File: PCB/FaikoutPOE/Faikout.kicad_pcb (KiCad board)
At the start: 2 copper layers, 39 x 65 mm, 91 parts, among them J1 RJ45_LED, J3 S21, J5 Reset, J7 TC2030-USB-NL-DS, M1 Ag9912-LP, P1 Square, P2 Square, P3 Square, P4 Square, P5 Square, P6 Square, P7 Square, P8 Square, Q1 BSS138PS, Q2 BSS138PS, U1 KSZ8851SNL, U2 ESP32-S3-MINI-1, U3 TCMT1100, U5 TCMT1100, U6 TPS62933, Y1 Crystal_GND24

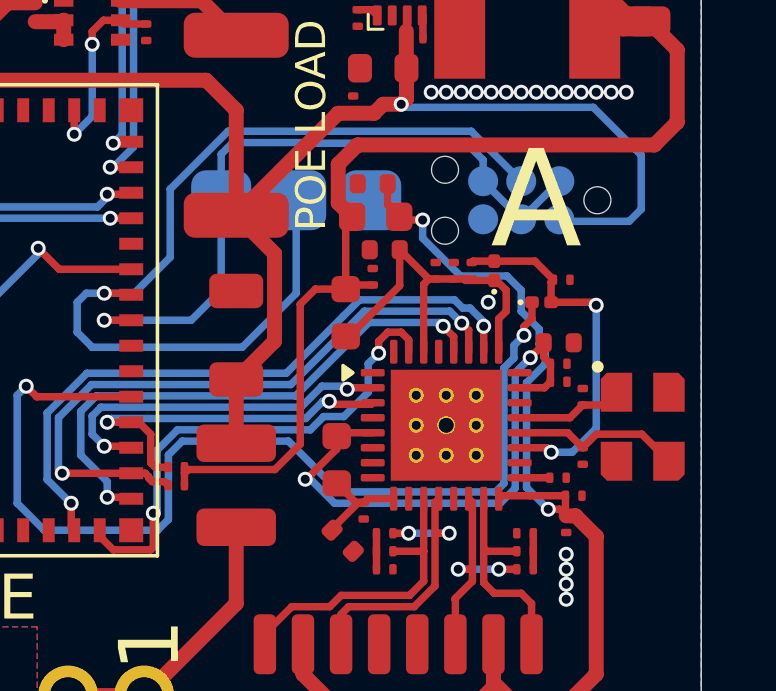
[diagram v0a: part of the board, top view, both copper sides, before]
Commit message: Revised Ethernet footprint
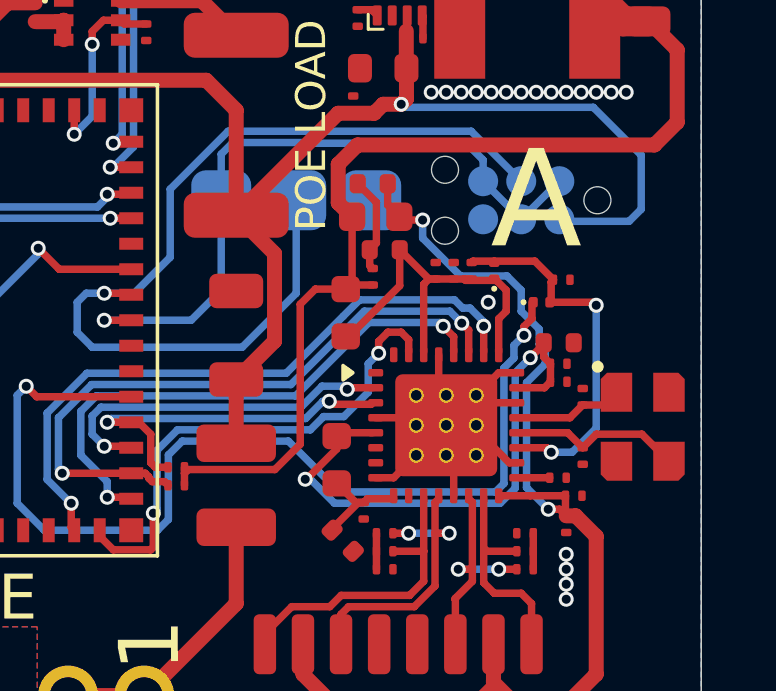
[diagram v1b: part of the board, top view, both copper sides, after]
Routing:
- net GND: track 0.77 -> 20.3 mm

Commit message: More work on Ethernet footprint
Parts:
- moved C18 0.20 mm to (128.2, 56.6)
- moved D1 0.12 mm to (133.8, 64.4)
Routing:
- net GND: track 20.3 -> 28.2 mm, vias 65 -> 72
- net D+: track 32.5 -> 33.2 mm
- net Net-(P1-P): track 5.56 -> 4.99 mm
